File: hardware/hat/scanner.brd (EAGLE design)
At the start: 65 x 56 mm, 26 parts, among them U1 CAT24C32WI-GT3, U2 TPS61165DBV

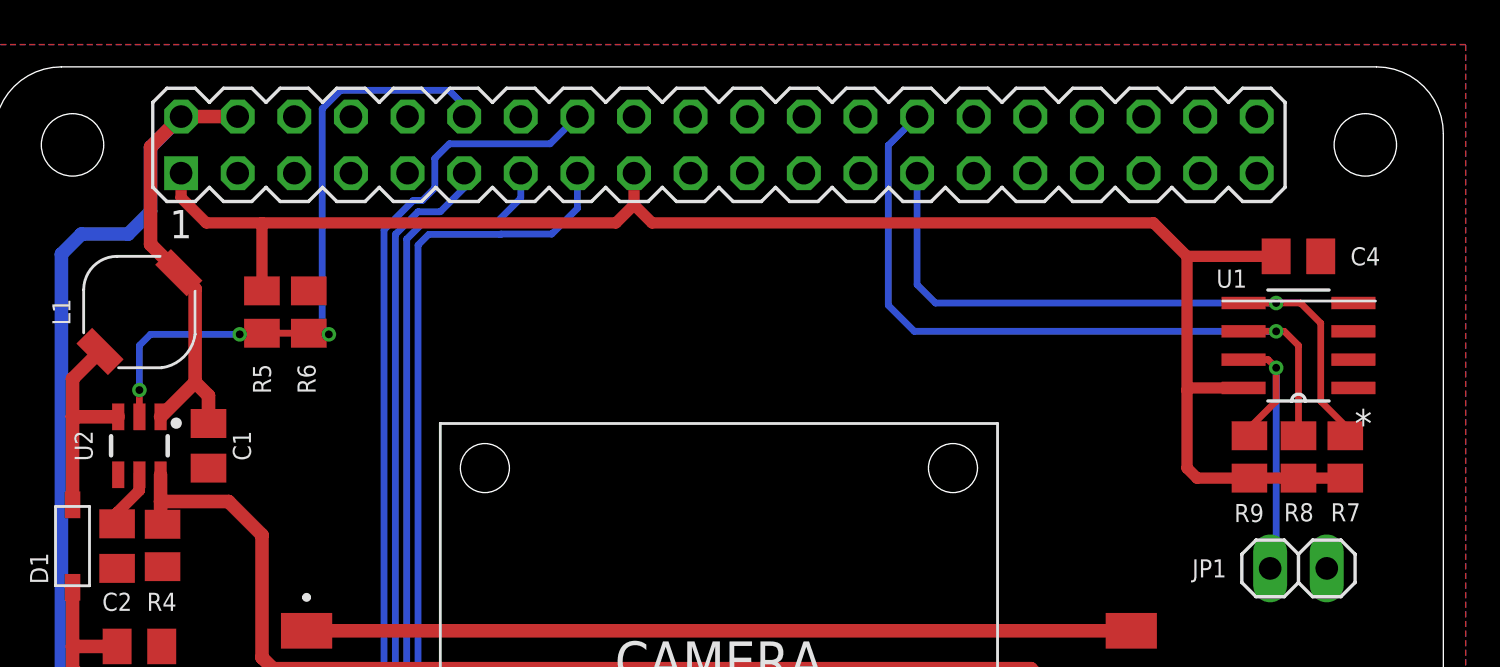
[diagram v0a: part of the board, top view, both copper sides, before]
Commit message: add 3V3 regulator
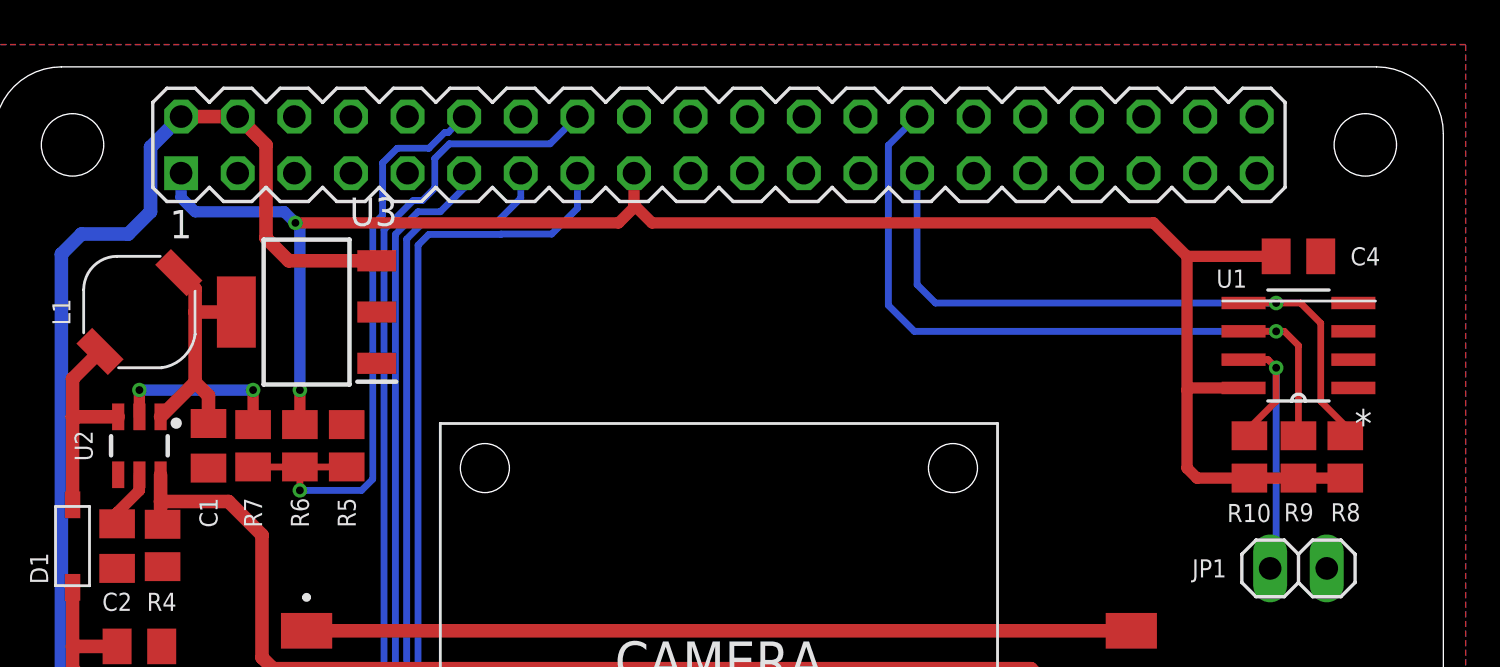
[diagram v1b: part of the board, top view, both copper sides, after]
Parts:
- added R10: 3k9, resistor:M0805
- added U3: LM1117MPX-3.3_NOPB, LM1117MPX-3.3_NOPB:SOT230P700X180-4N
- R7: value 3k9 -> (none)
- moved R7 49.0 mm to (-20.9, -13.5)
- moved R5 7.10 mm to (-16.7, -13.5), turned to 270 degrees
- moved R6 6.01 mm to (-18.8, -13.5), turned to 90 degrees
- moved R9 2.20 mm to (26.0, -14.0), turned to 270 degrees
- moved R8 2.10 mm to (28.1, -14.0)
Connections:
- new net LED_CTRL1: R7.1, U2.2
- new net VCC: C1.1, L1.1, U2.1, U3.4
- net +3V3: now also R10.1, R6.2, R9.2; no longer R5.2, R7.2, R9.1
- net +5V: now also U3.3; no longer C1.1, L1.1, U2.1
- net EEPROM_SCL: now also R9.1; no longer R8.1
- net EEPROM_SDA: now also R8.1; no longer R7.1
- net EEPROM_WP: now also R10.2; no longer R9.2
- net GND: now also R5.1, U3.1; no longer LED1.3, LED2.3, R6.1
- net LED_CTRL: now also R5.2, R6.1, R7.2; no longer R5.1, R6.2, U2.2
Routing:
- net VCC: track 0.00 -> 11.4 mm
- net LED_CTRL1: track 0.00 -> 7.85 mm, vias 0 -> 2
- net +5V: track 70.0 -> 63.7 mm
- net +3V3: track 75.8 -> 81.9 mm, vias 0 -> 2
- net LED_CTRL: track 29.7 -> 27.6 mm, vias 3 -> 1

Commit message: v1.1-d1
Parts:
- removed POWER: PJ-102AH, PJ-102AH:PJ-102AH
- added C5, C6: (no value), rcl:CT6032
- added J1: PJ-102AH, PJ-102AH:PJ-102AH
- R5, R6: value (none) -> Optional
- R7: value (none) -> 0
- U3: value LM1117MPX-3.3_NOPB -> (none); device LM1117MPX-3.3_NOPB:SOT230P700X180-4N -> SparkFun-IC-Power:SOT223
- moved LED1 1.00 mm to (-17.5, -27.0)
- moved LED2 1.00 mm to (17.5, -27.0)
- moved TRIGGER 0.81 mm to (-27.3, -29.4)
- moved C3 0.50 mm to (-26.0, -22.0)
- moved U3 0.50 mm to (-18.0, -7.50), turned to 90 degrees
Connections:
- net +5V: now also C6.+, J1.1; no longer POWER.1
- net GND: now also C5.-, C6.-, J1.2; no longer POWER.2, POWER.3
- net VCC: now also C5.+, U3.2
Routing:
- net VCC: track 11.4 -> 23.5 mm
- net +5V: track 63.7 -> 70.3 mm
- net LED_FB: track 59.2 -> 62.5 mm
- net N$3: track 37.0 -> 35.0 mm
- net N$2: track 23.3 -> 24.3 mm
- net TRIGGER: track 46.7 -> 45.8 mm

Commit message: .
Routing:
- net VCC: track 23.5 -> 24.2 mm
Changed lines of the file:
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@@
 <contactref element="L1" pad="1"/>
 <wire x1="-23.5" y1="-6.4644625" x2="-24.23223125" y2="-5.73223125" width="0.6096" layer="1"/>
-<wire x1="-23.5" y1="-10.1499" x2="-25.05" y2="-11.6999" width="0.6096" layer="1"/>
-<wire x1="-25.05" y1="-11.6999" x2="-25.05" y2="-12.1999" width="0.6096" layer="1"/>
-<wire x1="-23.5" y1="-10.1499" x2="-23.5" y2="-7.5" width="0.6096" layer="1"/>
 <wire x1="-23.5" y1="-7.5" x2="-23.5" y2="-6.4644625" width="0.6096" layer="1"/>
-<wire x1="-23.5" y1="-10.1499" x2="-22.9" y2="-10.7499" width="0.6096" layer="1"/>
-<wire x1="-22.9" y1="-10.7499" x2="-22.9" y2="-12.5" width="0.6096" layer="1"/>
 <contactref element="U3" pad="4"/>
 <contactref element="U3" pad="2"/>
@@
 <wire x1="-21.099" y1="-7.5" x2="-23.5" y2="-7.5" width="0.6096" layer="1"/>
 <wire x1="-14.9012" y1="-7.5" x2="-21.099" y2="-7.5" width="0.6096" layer="1"/>
-<wire x1="-14.9012" y1="-7.5" x2="-13.5" y2="-7.5" width="0.6096" layer="1"/>
-<wire x1="-13.5" y1="-7.5" x2="-11" y2="-5" width="0.6096" layer="1"/>
+<wire x1="-14.9012" y1="-7.5" x2="-12" y2="-7.5" width="0.6096" layer="1"/>
+<wire x1="-11" y1="-6.5" x2="-11" y2="-5" width="0.6096" layer="1"/>
+<wire x1="-11" y1="-6.5" x2="-12" y2="-7.5" width="0.6096" layer="1"/>
+<wire x1="-22.9" y1="-12.5" x2="-23" y2="-12.4" width="0.6096" layer="1"/>
+<wire x1="-23" y1="-12.4" x2="-23" y2="-11.5" width="0.6096" layer="1"/>
+<wire x1="-23" y1="-11.5" x2="-23.5" y2="-11" width="0.6096" layer="1"/>
+<wire x1="-23.5" y1="-11" x2="-24.5" y2="-11" width="0.6096" layer="1"/>
+<wire x1="-24.5" y1="-11" x2="-25.05" y2="-11.55" width="0.6096" layer="1"/>
+<wire x1="-25.05" y1="-11.55" x2="-25.05" y2="-12.1999" width="0.6096" layer="1"/>
+<wire x1="-23.5" y1="-7.5" x2="-23.5" y2="-11" width="0.6096" layer="1"/>
 </signal>
 </signals>
